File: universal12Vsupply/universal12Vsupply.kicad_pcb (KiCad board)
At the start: 2 copper layers, 44 parts, among them J1 Screw_Terminal_01x04, J2 Screw_Terminal_01x02, U1 LM5175PWP

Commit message: started PCB layout
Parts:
- added C7: 15u, Capacitor_SMD:C_1206_3216Metric_Pad1.33x1.80mm_HandSolder, F.Cu at (134.2, 48.1)
- added C8: 15u, Capacitor_SMD:C_1206_3216Metric_Pad1.33x1.80mm_HandSolder, F.Cu at (131.4, 48.1)
- added C9: 15u, Capacitor_SMD:C_1206_3216Metric_Pad1.33x1.80mm_HandSolder, F.Cu at (128.6, 48.1)
- moved H2 122.0 mm to (195.3, 19.0)
- moved Dboot2 112.1 mm to (173.5, 92.1)
- moved Dboot1 104.5 mm to (163.3, 92.1)
- moved D3 97.6 mm to (153.1, 92.2)
- moved Cc2 96.7 mm to (158.0, 71.2)
- moved D1 95.9 mm to (162.8, 36.5), turned to 90 degrees
- moved Cc1 94.8 mm to (156.2, 69.1)
- moved R5 93.1 mm to (150.6, 54.5), turned to 90 degrees
- moved R4 89.9 mm to (148.4, 54.5), turned to 90 degrees
- moved Rc1 89.9 mm to (159.8, 69.1)
- moved Css1 88.8 mm to (146.4, 66.9), turned to -90 degrees
- moved Cslope1 86.2 mm to (144.7, 66.9), turned to -90 degrees
- moved Rmode1 74.0 mm to (141.1, 66.9), turned to 90 degrees
- moved RT1 73.7 mm to (142.8, 66.9), turned to -90 degrees
- moved D2 66.9 mm to (132.8, 29.2)
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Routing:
- net /source2_4: track 0.00 -> 39.5 mm, vias 0 -> 1
- net GND: track 0.00 -> 33.9 mm, vias 0 -> 6
- net HDRV1: track 0.00 -> 28.5 mm
- net LDRV2: track 0.00 -> 20.4 mm
- net LDRV1: track 0.00 -> 18.9 mm
- net SW2: track 0.00 -> 17.6 mm
- net HDRV2: track 0.00 -> 13.8 mm
- net /SS: track 0.00 -> 2.97 mm
- net /RT/SYNC: track 0.00 -> 2.94 mm
- net /COMP: track 0.00 -> 2.89 mm
- net /SLOPE: track 0.00 -> 2.53 mm
- net Net-(Cc1-Pad2): track 0.00 -> 1.78 mm
- added copper zone on B.Cu, net GND
- added copper zone on F.Cu, net SW1
- added copper zone on F.Cu, net SW2

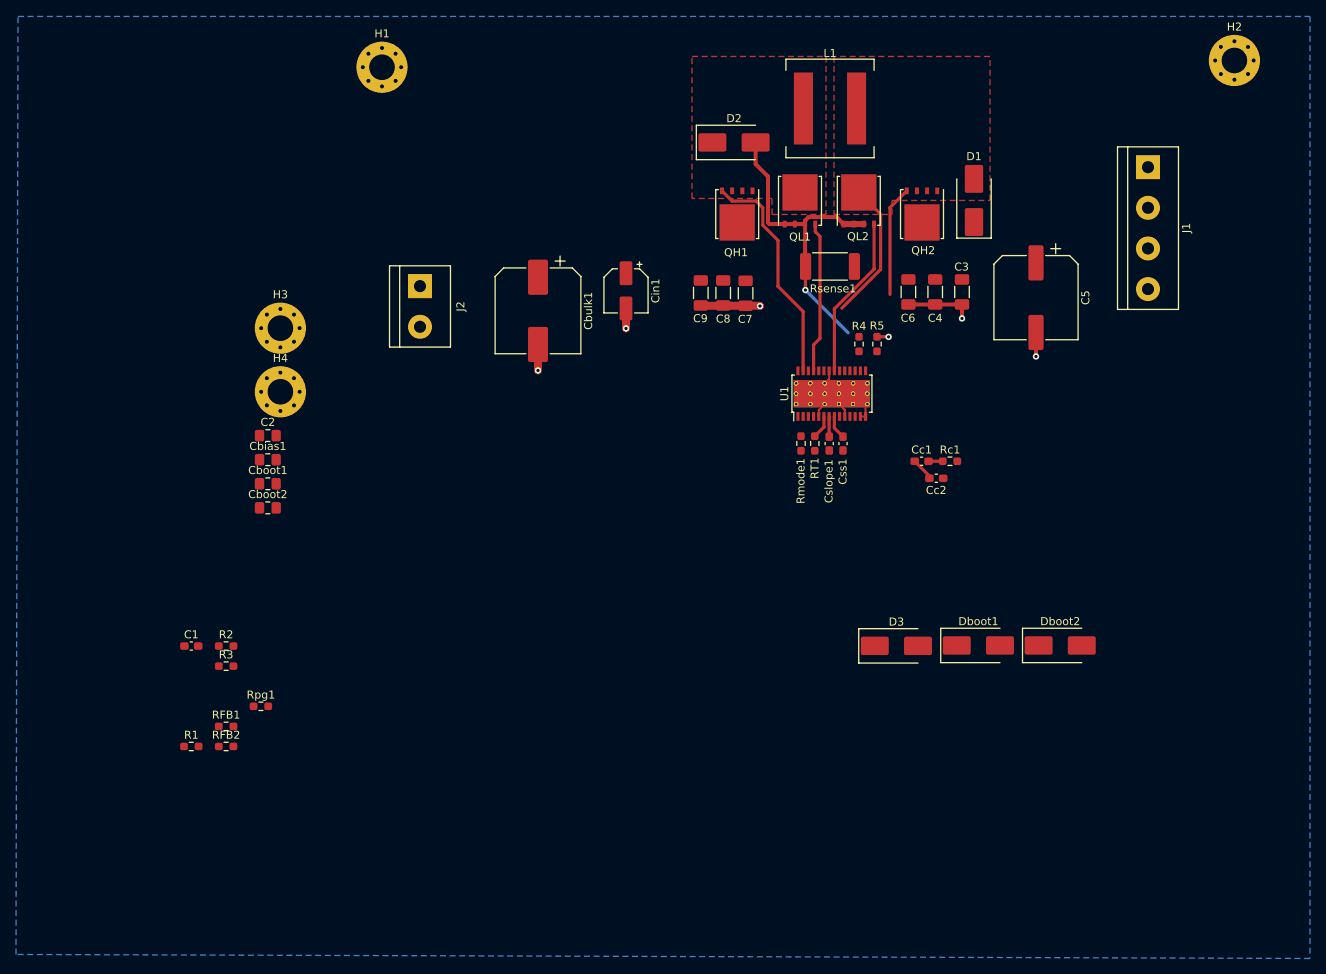
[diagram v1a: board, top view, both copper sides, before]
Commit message: 'finalised' layout without DRC errors
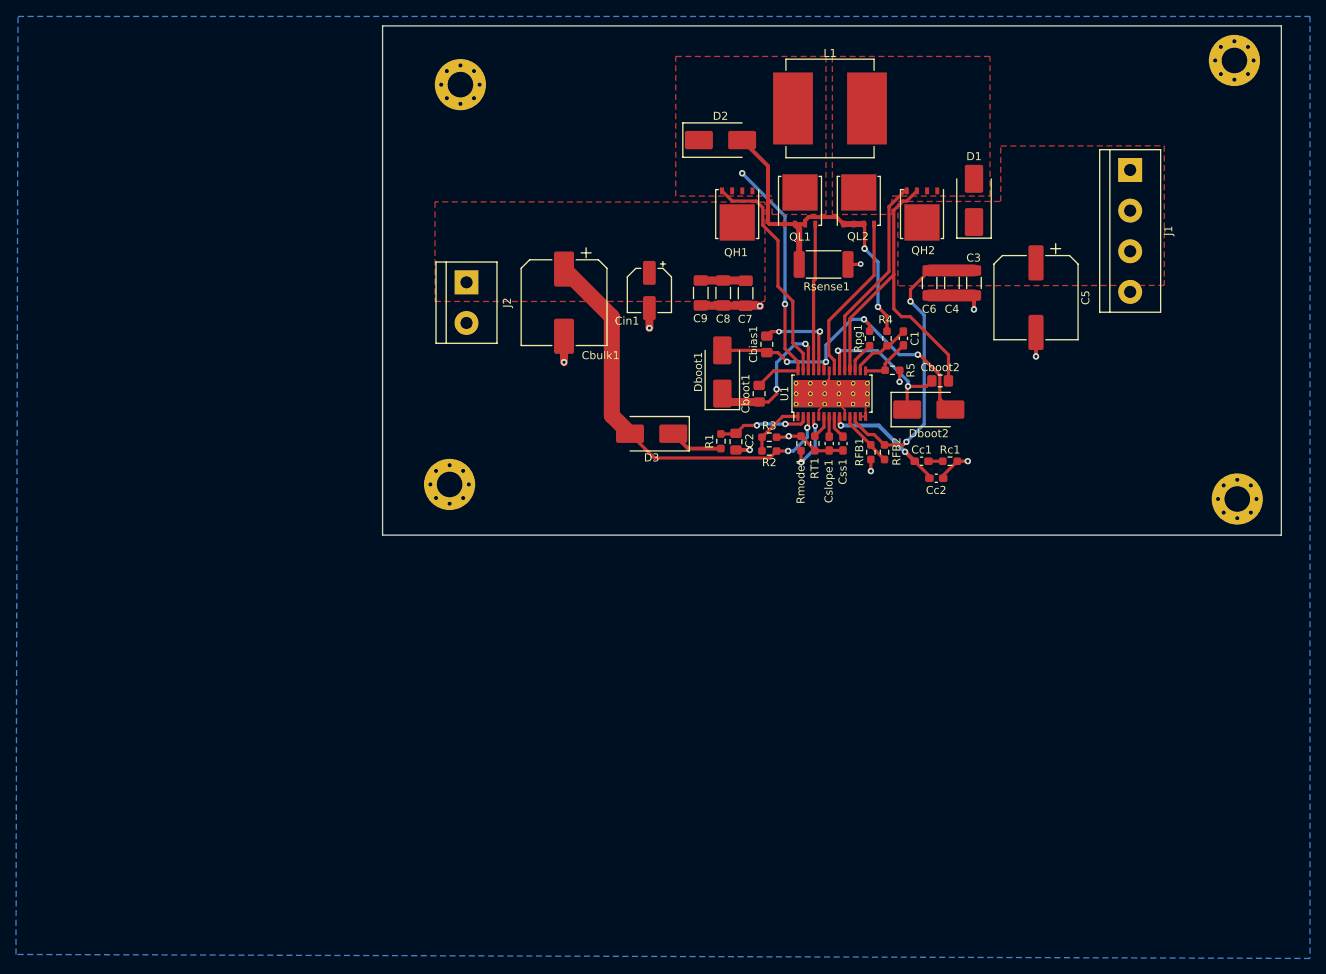
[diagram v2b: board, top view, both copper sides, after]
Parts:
- L1: footprint Inductor_SMD:L_Coilcraft_XAL1010-XXX -> FootprintLibrary:L_Coilcraft_XAL1010-XXX_handsolder
- moved H4 120.4 mm to (195.7, 73.8)
- moved C1 97.0 mm to (153.9, 53.7), turned to -90 degrees
- moved RFB2 90.1 mm to (151.6, 68.0), turned to -90 degrees
- moved Rpg1 88.9 mm to (149.7, 53.8), turned to 90 degrees
- moved RFB1 87.6 mm to (149.9, 68.0), turned to -90 degrees
- moved Cboot2 85.5 mm to (158.5, 59.1)
- moved R1 76.4 mm to (131.1, 66.6), turned to 90 degrees
- moved R3 73.7 mm to (137.2, 66.1)
- moved R2 72.1 mm to (137.2, 67.8), turned to 180 degrees
- moved Cbias1 64.0 mm to (136.9, 54.5), turned to 90 degrees
- moved Cboot1 62.4 mm to (135.9, 60.7), turned to 90 degrees
- moved C2 58.5 mm to (133.0, 66.6), turned to -90 degrees
- moved Dboot1 46.8 mm to (131.3, 57.9), turned to 90 degrees
- moved D3 40.5 mm to (122.5, 65.7), turned to 180 degrees
- moved Dboot2 33.8 mm to (157.1, 62.6)
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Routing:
- net Vin: track 0.00 -> 56.8 mm, vias 0 -> 2
- net Vcc: track 0.00 -> 42.3 mm, vias 0 -> 4
- net Vout: track 0.00 -> 38.0 mm, vias 0 -> 2
- net SW1: track 0.00 -> 33.2 mm, vias 0 -> 2
- net SW2: track 17.6 -> 43.7 mm
- net /BOOT2: track 0.00 -> 19.8 mm, vias 0 -> 2
- net /BOOT1: track 0.00 -> 19.7 mm, vias 0 -> 2
- net GND: track 33.9 -> 50.9 mm, vias 6 -> 11
- net /COMP: track 2.89 -> 15.2 mm, vias 0 -> 2
- net HDRV2: track 13.8 -> 25.9 mm
- net /BIAS: track 0.00 -> 11.9 mm, vias 0 -> 2
- net ICVin: track 0.00 -> 11.6 mm, vias 0 -> 2
- net /MODE: track 0.00 -> 8.01 mm, vias 0 -> 2
- net CS: track 0.24 -> 7.81 mm
- net EN: track 0.00 -> 7.30 mm
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- added copper zone on F.Cu, net Vin
- added copper zone on F.Cu, net Vout
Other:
- board outline added: 112.3 x 63.7 mm

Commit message: design clean up
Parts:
- added TP1: TestPoint, TestPoint:TestPoint_THTPad_2.5x2.5mm_Drill1.2mm, F.Cu at (133.5, 24.0)
- added TP10: TestPoint, TestPoint:TestPoint_THTPad_2.5x2.5mm_Drill1.2mm, F.Cu at (179.4, 21.0)
- added TP11: TestPoint, TestPoint:TestPoint_THTPad_2.5x2.5mm_Drill1.2mm, F.Cu at (113.0, 73.0)
- added TP12: TestPoint, TestPoint:TestPoint_THTPad_2.5x2.5mm_Drill1.2mm, F.Cu at (113.0, 21.0)
- added TP13: TestPoint, TestPoint:TestPoint_THTPad_2.5x2.5mm_Drill1.2mm, F.Cu at (179.5, 73.0)
- added TP14: TestPoint, TestPoint:TestPoint_THTPad_2.5x2.5mm_Drill1.2mm, F.Cu at (174.8, 28.6)
- added TP15: TestPoint, TestPoint:TestPoint_THTPad_2.5x2.5mm_Drill1.2mm, F.Cu at (113.0, 27.0)
- added TP2: TestPoint, TestPoint:TestPoint_THTPad_2.5x2.5mm_Drill1.2mm, F.Cu at (155.8, 24.6)
- added TP3: TestPoint, TestPoint:TestPoint_THTPad_2.5x2.5mm_Drill1.2mm, F.Cu at (126.8, 60.8)
- added TP4: TestPoint, TestPoint:TestPoint_THTPad_2.5x2.5mm_Drill1.2mm, F.Cu at (166.2, 62.6)
- added TP5: TestPoint, TestPoint:TestPoint_THTPad_2.5x2.5mm_Drill1.2mm, F.Cu at (127.0, 38.2)
- added TP6: TestPoint, TestPoint:TestPoint_THTPad_2.5x2.5mm_Drill1.2mm, F.Cu at (133.5, 19.8)
- added TP7: TestPoint, TestPoint:TestPoint_THTPad_2.5x2.5mm_Drill1.2mm, F.Cu at (126.8, 55.5)
- added TP8: TestPoint, TestPoint:TestPoint_THTPad_2.5x2.5mm_Drill1.2mm, F.Cu at (155.8, 29.2)
- added TP9: TestPoint, TestPoint:TestPoint_THTPad_2.5x2.5mm_Drill1.2mm, F.Cu at (155.8, 19.8)
- moved J2 14.5 mm to (110.2, 37.1), turned to 90 degrees
- moved H4 9.89 mm to (185.8, 73.0)
- moved H2 9.71 mm to (185.8, 21.0)
- moved H3 9.35 mm to (106.5, 73.0)
- moved H1 8.01 mm to (106.5, 21.0)
- moved J1 4.08 mm to (181.8, 28.6)
- moved Cboot1 0.11 mm to (136.0, 60.7)
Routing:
- net LDRV1: track 18.4 -> 36.5 mm, vias 0 -> 1
- net LDRV2: track 21.0 -> 38.1 mm
- net ICVin: track 11.6 -> 18.9 mm
- net HDRV2: track 25.9 -> 32.6 mm
- net Vcc: track 42.3 -> 48.7 mm
- net HDRV1: track 28.5 -> 34.4 mm
- net /source2_4: track 44.5 -> 49.6 mm
- net SW1: track 33.2 -> 35.5 mm
- net GND: vias 11 -> 13
- added copper zone on F.Cu, net GND
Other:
- board size 112.3 x 63.7 mm -> 88.3 x 60.8 mm
- board text added: "{ "ViaStitching": "0.2", "stitch_zone_0": { "HSpacing": "1", "VSpacing": "1", "Clearance": "0", "Randomize": false } }"

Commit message: added test points properly, DRC and ERC is fine
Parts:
- TP1: value TestPoint -> LDRV2
- TP10: value TestPoint -> Vin
- TP11, TP12, TP13, TP14: value TestPoint -> gnd
- TP15: value TestPoint -> source2_4
- TP2: value TestPoint -> ICVin
- TP3: value TestPoint -> Vcc
- TP4: value TestPoint -> HDRV1
- TP5: value TestPoint -> SW1
- TP6: value TestPoint -> LDRV1
- TP7: value TestPoint -> HDRV2
- TP8: value TestPoint -> SW2
- TP9: value TestPoint -> Vout
- moved TP10 66.7 mm to (113.0, 27.0)
- moved TP13 52.0 mm to (179.5, 21.0)
- moved TP2 46.4 mm to (126.8, 60.8)
- moved TP4 46.1 mm to (127.0, 38.2)
- moved TP14 44.6 mm to (179.5, 73.0)
- moved TP3 39.5 mm to (166.2, 62.5)
- moved TP7 39.1 mm to (155.8, 29.2)
- moved TP6 36.4 mm to (126.8, 55.5)
- moved TP1 22.3 mm to (155.8, 24.5)
- moved TP9 20.9 mm to (174.8, 28.5)
- moved TP15 20.7 mm to (133.5, 24.0)
- moved TP5 19.6 mm to (133.5, 19.8)
- moved TP8 9.45 mm to (155.8, 19.8)
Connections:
- TP1 pad 1: /source2_4 -> LDRV2
- TP10 pad 1: GND -> Vin
- TP14 pad 1: Vout -> GND
- TP15 pad 1: Vin -> /source2_4
- TP2 pad 1: LDRV2 -> ICVin
- TP3 pad 1: ICVin -> Vcc
- TP4 pad 1: Vcc -> HDRV1
- TP5 pad 1: HDRV1 -> SW1
- TP6 pad 1: SW1 -> LDRV1
- TP7 pad 1: LDRV1 -> HDRV2
- TP8 pad 1: HDRV2 -> SW2
- TP9 pad 1: SW2 -> Vout

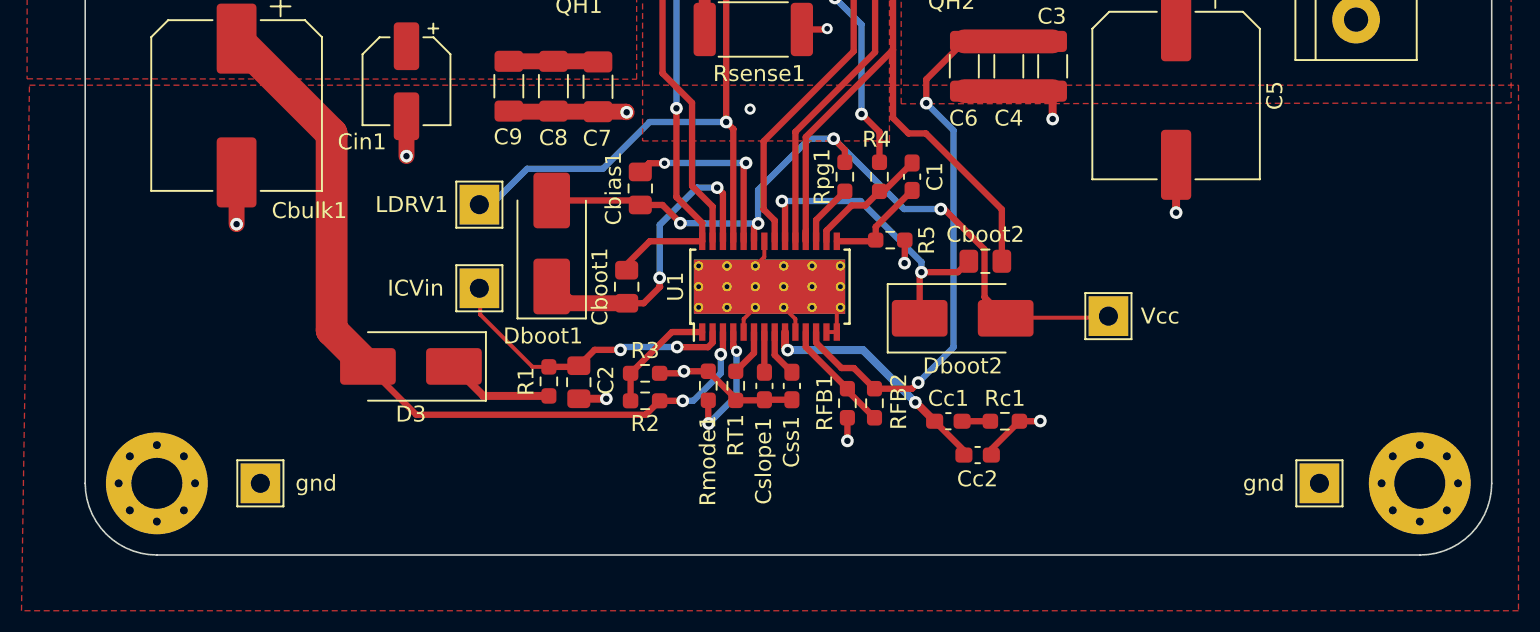
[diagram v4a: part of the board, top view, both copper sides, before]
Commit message: added via stiching
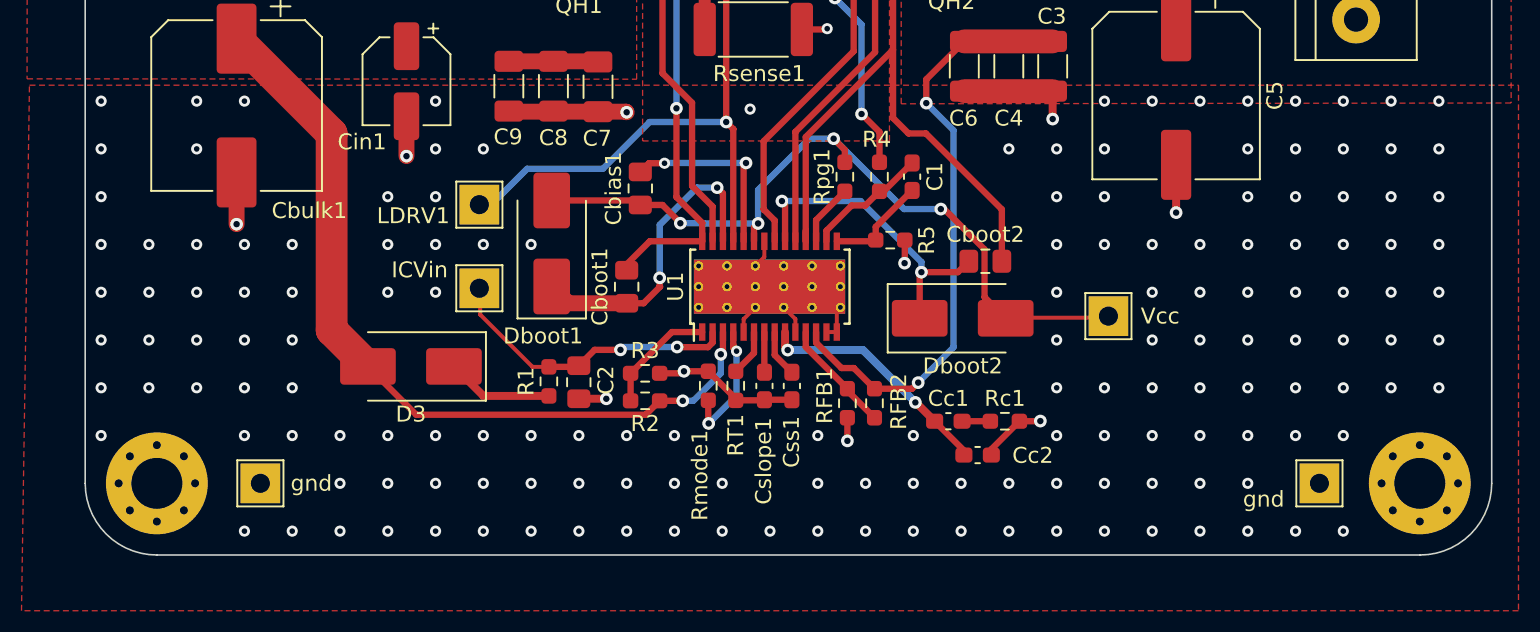
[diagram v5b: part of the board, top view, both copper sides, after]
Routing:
- net GND: vias 13 -> 170

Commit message: increased via stiching spacing
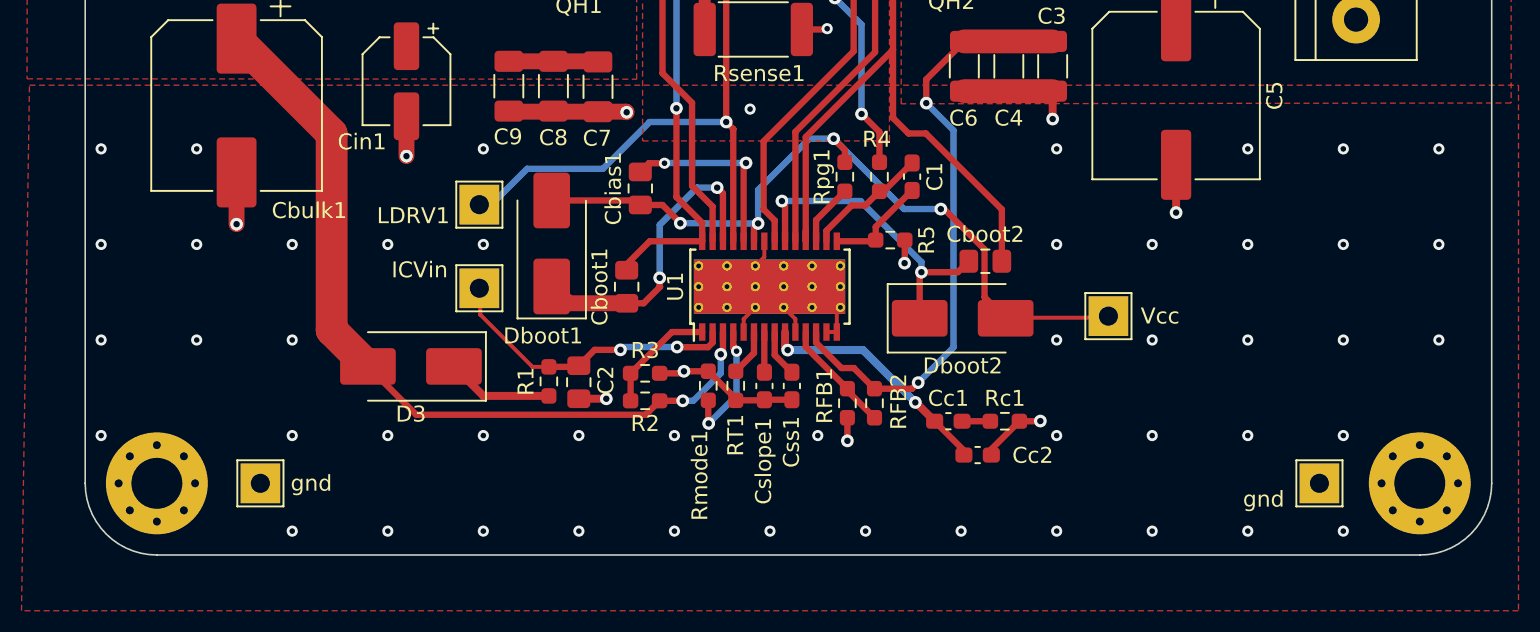
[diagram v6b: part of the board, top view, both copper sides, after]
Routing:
- net GND: vias 170 -> 61

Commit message: finished PCB
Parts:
- added Cbias1: 100n, Capacitor_SMD:C_0805_2012Metric_Pad1.18x1.45mm_HandSolder, F.Cu at (109.8, 68.0)
- moved TP14 46.6 mm to (133.2, 78.4)
- moved TP13 46.4 mm to (133.4, 26.6)
- moved TP9 45.5 mm to (129.6, 34.0)
- moved C2 43.4 mm to (90.0, 72.1)
- moved C3 43.4 mm to (119.7, 52.3)
- moved C6 43.4 mm to (114.2, 52.3)
- moved R5 43.4 mm to (109.5, 63.2)
- moved RFB1 43.4 mm to (106.9, 73.5)
- moved C1 43.4 mm to (110.9, 59.2)
- moved C5 43.4 mm to (127.5, 54.1)
- moved C8 43.4 mm to (88.4, 53.6)
- moved C9 43.4 mm to (85.6, 53.6)
- moved Cboot1 43.4 mm to (93.0, 66.2)
- moved Cboot2 43.4 mm to (115.5, 64.6)
- moved Cbulk1 43.4 mm to (68.5, 54.8)
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- renumbered Cbias1 to Cvcc1
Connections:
- Cvcc1 pad 2: /BIAS -> GND
- U1 pad 24: /BIAS -> Vout
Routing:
- net Vout: track 38.0 -> 59.5 mm, vias 2 -> 3
- net /BIAS: track 11.9 -> 0.00 mm, vias 2 -> 0
- net SW1: track 35.5 -> 33.3 mm
- net GND: track 50.9 -> 52.6 mm
- net /BOOT2: track 19.8 -> 21.3 mm
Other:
- board text added: "12V"
- board text added: "Vin"
- board text added: "gnd"
- board text removed: "{ "ViaStitching": "0.2", "stitch_zone_0": { "HSpacing": "1", "VSpacing": "1", "Clearance": "0", "Randomize": false } }"
